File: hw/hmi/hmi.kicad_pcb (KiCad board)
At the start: 2 copper layers, 118 parts, among them J1 SWD, J2 INTERFACE, J3 GPS, J4 SSD1963_LCD, J5 USB, J6 Antenna, J7 SD_Card, Q1 BC847, SW2 BTL1, SW3 BTL2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

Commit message: Added HMI and SDU boards
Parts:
- removed D5: Vadc, LED_SMD:LED_1206_3216Metric
- removed R15: 220, Resistor_SMD:R_0805_2012Metric
- removed R9: 10k, Resistor_SMD:R_0805_2012Metric
- removed the REF** at (75.2, 48.4)
- removed the REF** at (249.2, 48.4)
- removed the REF** at (75.2, 146.4)
- removed the REF** at (249.2, 146.4)
- added C40: 100n, Capacitor_SMD:C_0805_2012Metric, F.Cu at (162.7, 142.2)
- added JP2: MODEL2, Jumper:SolderJumper-2_P1.3mm_Open_TrianglePad1.0x1.5mm, F.Cu at (213.7, 79.0)
- added R38: 10k, Resistor_SMD:R_0805_2012Metric, F.Cu at (182.0, 92.0)
- added REF**: MountingHole_3.2mm_M3, MountingHole:MountingHole_3.2mm_M3, F.Cu at (213.2, 145.6)
- added REF**: MountingHole_3.2mm_M3, MountingHole:MountingHole_3.2mm_M3, F.Cu at (213.2, 67.6)
- added REF**: MountingHole_3.2mm_M3, MountingHole:MountingHole_3.2mm_M3, F.Cu at (85.7, 145.6)
- added REF**: MountingHole_3.2mm_M3, MountingHole:MountingHole_3.2mm_M3, F.Cu at (85.7, 67.6)
- C12: moved to B.Cu
- C20: value 50u -> 10u; footprint Capacitor_SMD:CP_Elec_6.3x7.7 -> Capacitor_SMD:C_0805_2012Metric
- C37: value 10n -> 100u; footprint Capacitor_SMD:C_0805_2012Metric -> Capacitor_SMD:CP_Elec_6.3x7.7
- J1: footprint Connector_PinHeader_2.54mm:PinHeader_1x05_P2.54mm_Vertical -> Connector_PinHeader_2.54mm:PinHeader_1x05_P2.54mm_Horizontal
- J2: footprint Connector_Dsub:DSUB-9_Female_Horizontal_P2.77x2.84mm_EdgePinOffset9.90mm_Housed_MountingHolesOffset11.32mm -> Connector_Dsub:DSUB-9_Female_Vertical_P2.77x2.84mm_MountingHoles; moved to B.Cu
- J5: footprint Connector_USB:USB_B_TE_5787834_Vertical -> Connector_USB:USB_A_Molex_105057_Vertical
- J6: footprint Connector_Coaxial:SMA_Amphenol_132289_EdgeMount -> Connector_Coaxial:SMA_Amphenol_132134-11_Vertical; moved to B.Cu
- J7: value SD_Card -> Micro_SD_Card_Det_Hirose_DM3AT; footprint Connector_Card:SD_TE_2041021 -> Connector_Card:microSD_HC_Hirose_DM3AT-SF-PEJM5
- moved J5 322.9 mm to (146.0, 154.9)
- moved C37 314.7 mm to (162.1, 131.1), turned to 90 degrees
- moved C24 308.5 mm to (160.5, 141.6), turned to 270 degrees
- moved U2 307.9 mm to (157.9, 146.0), turned to 180 degrees
- moved R7 307.8 mm to (163.9, 147.1)
- moved F1 305.6 mm to (159.0, 151.3), turned to 90 degrees
- moved C22 301.4 mm to (158.6, 141.6), turned to 270 degrees
- moved JP1 298.1 mm to (149.0, 143.3), turned to 90 degrees
- moved R13 297.0 mm to (146.4, 143.4), turned to 90 degrees
- moved R8 284.0 mm to (163.9, 145.1)
- moved C30 276.2 mm to (173.7, 95.4)
- moved U5 275.6 mm to (172.3, 92.9)
- moved C29 270.7 mm to (174.6, 92.7), turned to 90 degrees
- moved R10 269.9 mm to (171.7, 90.7)
- moved C27 268.8 mm to (173.7, 112.9), turned to 270 degrees
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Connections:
- C37 pad 1: /SD_DETECT -> +5V
- J4 pad 5: +5V -> Net-(J4-Pad5)
- J7 pad 1: /SDIO_D3 -> /SDIO_D2
- J7 pad 10: /SD_DETECT -> Net-(J7-Pad10)
- J7 pad 11: (no net) -> GND
- J7 pad 2: /SDIO_CMD -> /SDIO_D3
- J7 pad 3: GND -> /SDIO_CMD
- J7 pad 9: /SDIO_D2 -> GND
- R24 pad 2: /SD_DETECT -> Net-(J7-Pad10)
- U1 pad 15: /ADC_5V -> (no net)
- U1 pad 24: (no net) -> /ADC_5V
- U1 pad 25: /GPS_TX -> /DEBUG_TX
- U1 pad 26: /GPS_RX -> /DEBUG_RX
- U1 pad 31: /BUZZER -> (no net)
- U1 pad 47: /LCD_SD_CS -> (no net)
- U1 pad 64: (no net) -> /LCD_SD_CS
- U1 pad 68: /DEBUG_TX -> /GPS_TX
- U1 pad 69: /DEBUG_RX -> /GPS_RX
- U1 pad 90: (no net) -> /BUZZER
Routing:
- net +3V3: track 0.00 -> 720.9 mm, vias 0 -> 6
- net GND: track 0.00 -> 344.4 mm, vias 0 -> 28
- net +5V: track 0.00 -> 298.5 mm, vias 0 -> 4
- net /RESET: track 0.00 -> 142.0 mm, vias 0 -> 1
- net /SDIO_D0: track 0.00 -> 131.3 mm
- net /SDIO_D1: track 0.00 -> 131.1 mm, vias 0 -> 2
- net Net-(R25-Pad2): track 0.00 -> 128.9 mm
- net /SWDIO: track 0.00 -> 128.7 mm, vias 0 -> 2
- net /SWCLK: track 0.00 -> 123.8 mm, vias 0 -> 2
- net /SDIO_D3: track 0.00 -> 121.5 mm, vias 0 -> 2
- net /SDIO_D2: track 0.00 -> 120.7 mm, vias 0 -> 2
- net /SDIO_CMD: track 0.00 -> 120.5 mm
- net /LED_SYS_ACT: track 0.00 -> 118.4 mm, vias 0 -> 2
- net Net-(R26-Pad2): track 0.00 -> 114.0 mm
- net /SDIO_CLK: track 0.00 -> 108.2 mm
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- added copper zone on B.Cu, net GND
- added copper zone on F.Cu, net GND
- added copper zone on F.Cu, net Net-(C33-Pad1)
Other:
- board outline added: 133.5 x 95 mm
- rule trace_min: 0.2 -> 0.25
- board text added: "868 MHz Antenna"
- board text added: "BUT FME BUT FEEC"
- board text added: "CR2032"
- board text added: "GPS 3.3 R T GND"
- board text added: "Pneumobil HMI v0.1 Jakub Kaderka 2018"
- board text added: "SWD"

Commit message: Updated power supply in HMI
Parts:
- added C41: 100n, Capacitor_SMD:C_0805_2012Metric, F.Cu at (177.2, 139.5)
- added C42: 10u, Capacitor_SMD:C_0805_2012Metric, F.Cu at (173.8, 140.6)
- moved L1 20.6 mm to (191.3, 139.4), turned to 270 degrees
- moved U8 15.1 mm to (186.3, 139.1), turned to 0 degrees
- moved C31 15.0 mm to (186.5, 136.3)
- moved C35 14.5 mm to (187.1, 141.9), turned to 180 degrees
- moved U7 12.8 mm to (175.7, 132.9), turned to 90 degrees
- moved C33 8.08 mm to (173.8, 138.6), turned to 180 degrees
- moved D8 6.20 mm to (180.4, 136.1)
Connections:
- C18 pad 1: +3V3 -> +3.3VP
- C19 pad 1: +3V3 -> +3.3VP
- C33 pad 1: Net-(C33-Pad1) -> +3V3
- C35 pad 1: +3V3 -> +3.3VP
- J4 pad 37: +3V3 -> +3.3VP
- L1 pad 2: +3V3 -> +3.3VP
- L2 pad 1: Net-(C33-Pad1) -> +3V3
- U7 pad 2: Net-(C33-Pad1) -> +3V3
- U8 pad 4: +3V3 -> +3.3VP
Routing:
- net +3.3VP: track 0.00 -> 43.4 mm, vias 0 -> 2
- net Net-(C33-Pad1): track 24.7 -> 0.00 mm
- net +5V: track 298.5 -> 321.9 mm
- net GND: track 344.4 -> 358.1 mm, vias 28 -> 30
- net +3V3: track 720.9 -> 711.1 mm, vias 6 -> 4
- net Net-(L1-Pad1): track 0.00 -> 7.56 mm
- net /DEBUG_TX: track 86.6 -> 84.3 mm
- net /RESET: track 142.0 -> 143.1 mm, vias 1 -> 2
- added copper zone on F.Cu, net +3V3
- added copper zone on F.Cu, net +5V
- removed copper zone on F.Cu, net Net-(C33-Pad1)

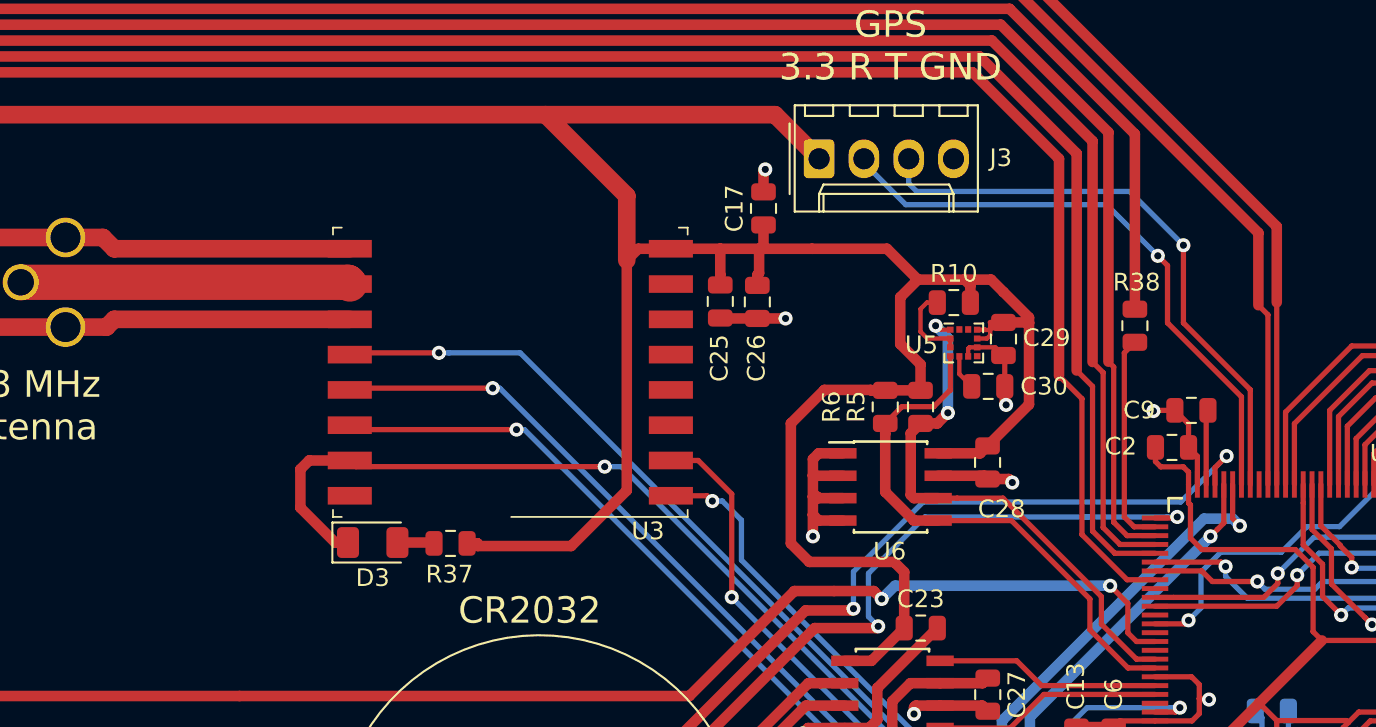
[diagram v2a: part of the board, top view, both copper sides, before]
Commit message: Added pressure sensor to hmi
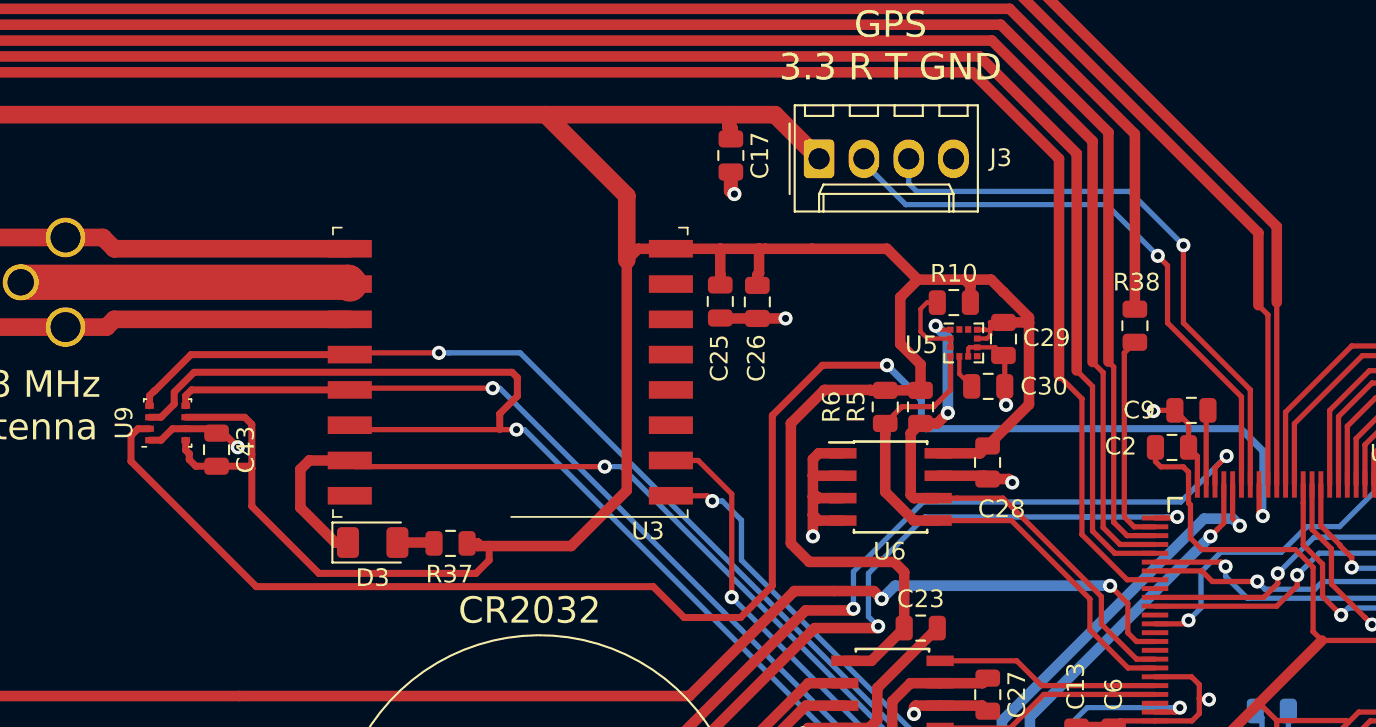
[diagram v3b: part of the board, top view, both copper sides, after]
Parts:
- added C43: 100n, Capacitor_SMD:C_0805_2012Metric, F.Cu at (129.9, 99.0)
- added U9: BME280, Package_LGA:Bosch_LGA-8_2.5x2.5mm_P0.65mm_ClockwisePinNumbering, F.Cu at (127.2, 97.5)
- moved C17 3.52 mm to (159.1, 82.3), turned to 270 degrees
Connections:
- U1 pad 67: (no net) -> /BME_CS
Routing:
- net /BME_CS: track 0.00 -> 90.5 mm, vias 0 -> 2
- net +3V3: track 711.1 -> 740.7 mm
- net /SPI4_MOSI: track 62.5 -> 88.2 mm
- net /SPI4_SCK: track 58.6 -> 71.5 mm
- net /SPI4_MISO: track 61.9 -> 71.9 mm
- net GND: track 358.1 -> 363.8 mm, vias 30 -> 31

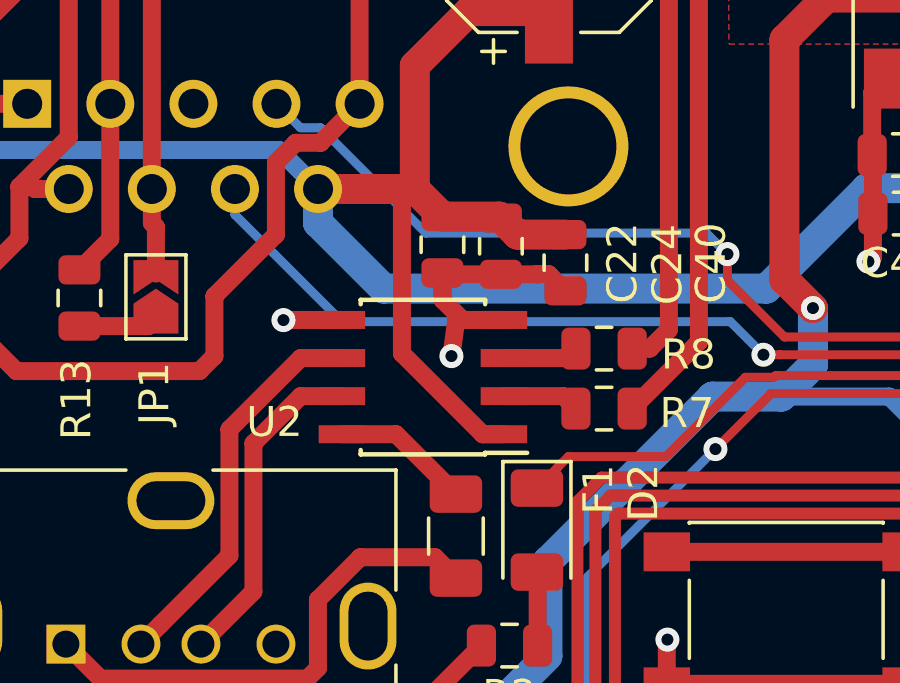
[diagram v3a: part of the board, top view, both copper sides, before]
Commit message: Updated schematic to latest changes in usb protection ic
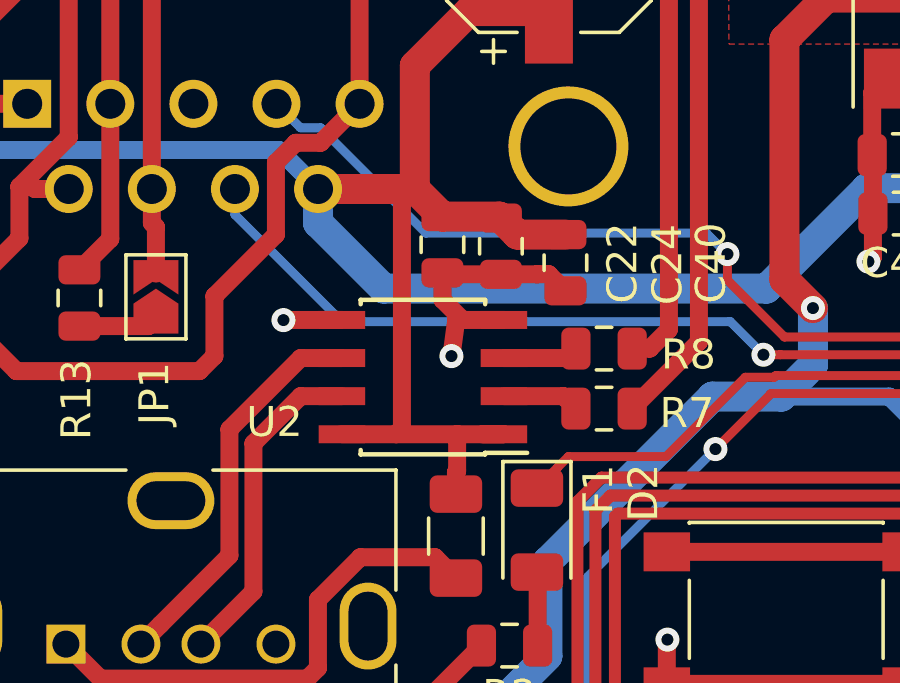
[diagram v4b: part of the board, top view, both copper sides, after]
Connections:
- F1 pad 2: Net-(F1-Pad2) -> +5V
- U2 pad 8: Net-(F1-Pad2) -> +5V
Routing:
- net +5V: track 321.9 -> 328.2 mm
- net Net-(F1-Pad2): track 4.63 -> 0.00 mm

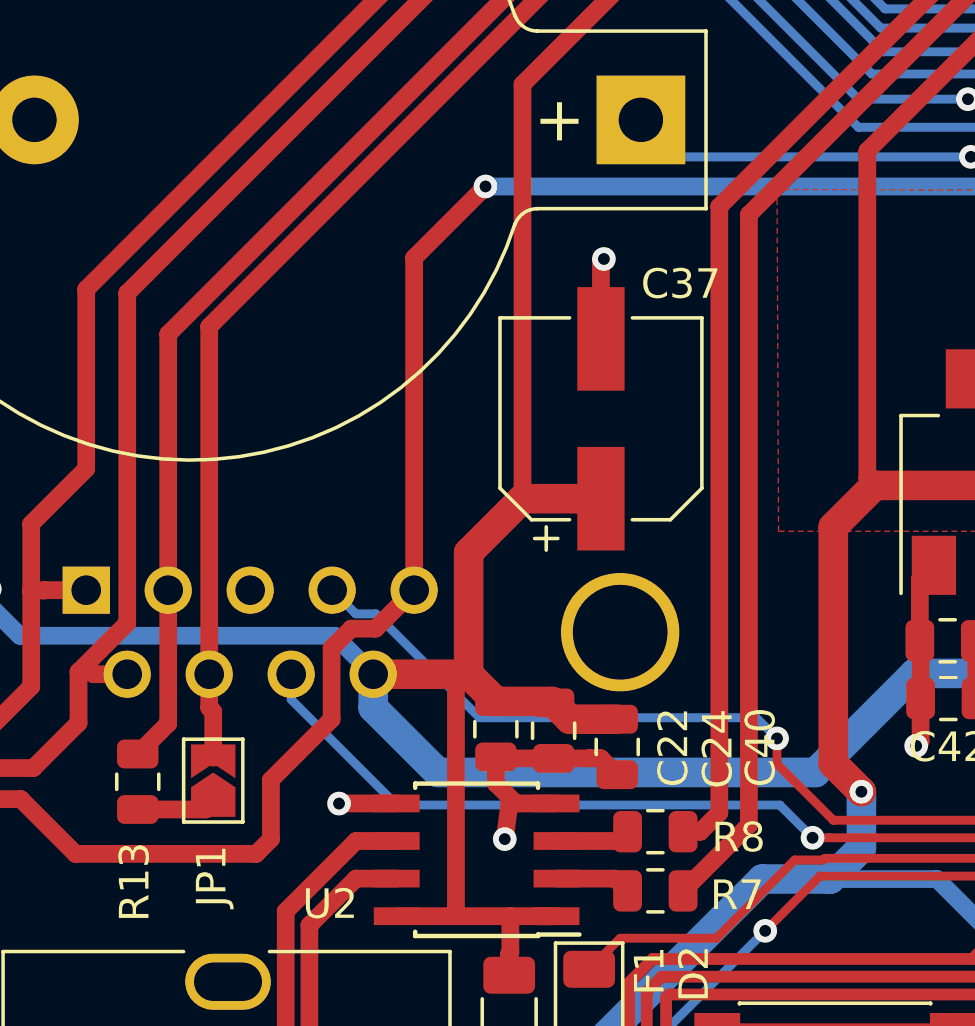
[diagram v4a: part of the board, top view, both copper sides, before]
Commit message: Made space around connectors screw for nut
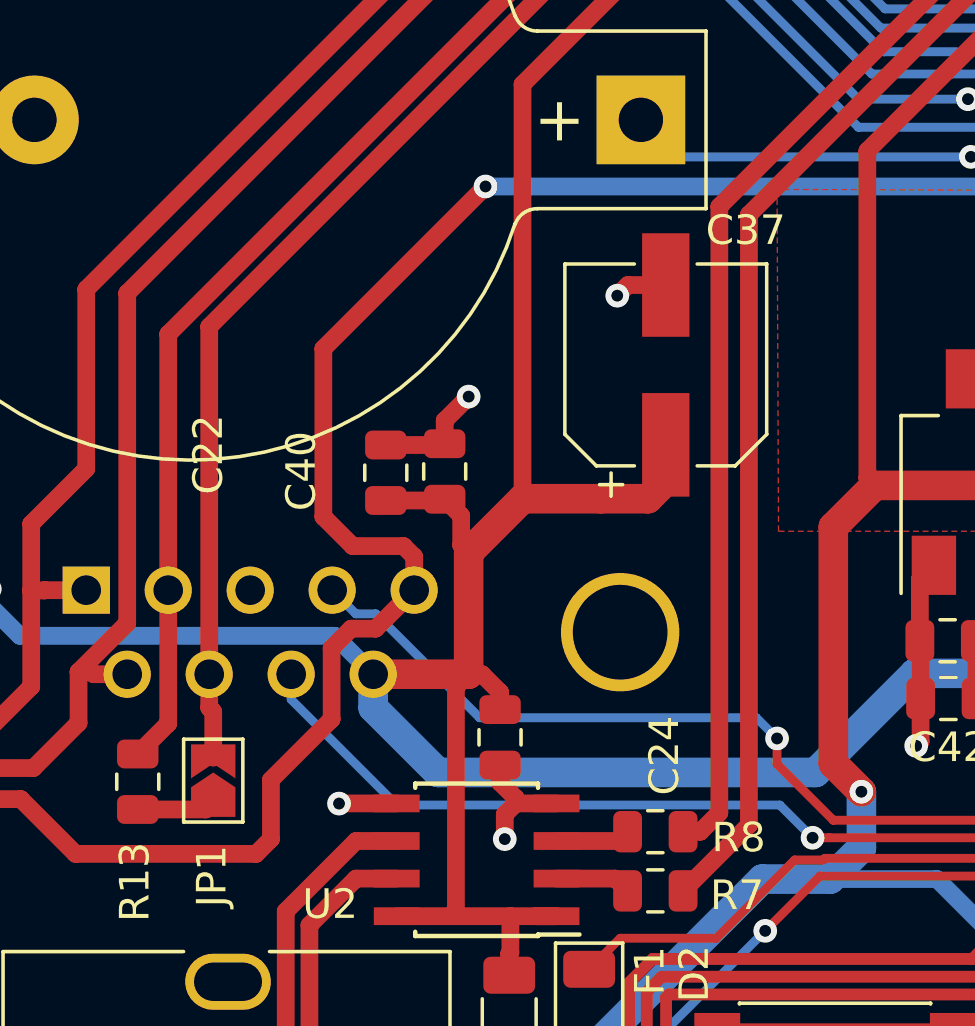
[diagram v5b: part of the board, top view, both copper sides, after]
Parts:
- moved C40 11.0 mm to (156.8, 132.9), turned to 90 degrees
- moved C22 9.43 mm to (154.8, 132.9), turned to 90 degrees
- moved C37 2.85 mm to (164.3, 129.3)
- moved C24 1.82 mm to (158.7, 141.9)
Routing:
- net +5V: track 328.2 -> 332.3 mm
- net /RESET: track 143.1 -> 146.6 mm
- net GND: track 363.8 -> 362.1 mm, vias 31 -> 32
